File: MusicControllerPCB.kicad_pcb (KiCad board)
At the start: 2 copper layers, 66 x 55.9 mm, 8 parts, among them SW1 SW_Push, SW2 SW_Push, SW3 SW_Push, SW4 SW_Push

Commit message: Some cleanup
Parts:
- removed A1: Arduino_Nano_v3.x, Module:Arduino_Nano
- added A101: Arduino_Nano_v3.x, Module:Arduino_Nano, B.Cu at (89.6, 72.2)
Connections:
- Brd1 pad 1: Net-(A1-+5V) -> GND
- Brd1 pad 2: Net-(A1-A5) -> +5V
- Brd1 pad 3: Net-(A1-A5) -> Net-(A101-A5)
- Brd1 pad 4: Net-(A1-A5) -> Net-(A101-A4)
- RotaryEncoder1 pad 1: Net-(A1-D11) -> /Rot_{CLK}
- RotaryEncoder1 pad 2: Net-(A1-D10) -> /Rot_{DT}
- RotaryEncoder1 pad 4: Net-(A1-A5) -> +5V
- RotaryEncoder1 pad 5: Net-(RotaryEncoder1-GND) -> GND
- SW1 pad 1: Net-(A1-+5V) -> GND
- SW2 pad 1: Net-(A1-+5V) -> GND
- SW3 pad 1: Net-(A1-+5V) -> GND
- SW4 pad 1: Net-(A1-+5V) -> GND
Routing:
- net Net-(A1-A5): track 164.1 -> 0.00 mm
- net Net-(A1-+5V): track 129.3 -> 0.00 mm
- net +5V: track 0.00 -> 74.6 mm
- net /Rot_{DT}: track 0.00 -> 74.0 mm
- net /Rot_{CLK}: track 0.00 -> 60.0 mm
- net Net-(A1-D10): track 41.7 -> 0.00 mm
- net Net-(RotaryEncoder1-GND): track 40.8 -> 0.00 mm
- net Net-(A1-D11): track 40.8 -> 0.00 mm
- net Net-(A101-A5): track 0.00 -> 31.1 mm
- net Net-(A101-A4): track 0.00 -> 28.7 mm
- net Net-(A101-D2): track 24.4 -> 46.1 mm
- net Net-(A101-D3): track 17.4 -> 29.3 mm
- net Net-(A101-D5): track 23.6 -> 14.8 mm
- net Net-(A101-D4): track 35.3 -> 40.7 mm
- added copper zone on B.Cu, net GND
- added copper zone on F.Cu, net GND
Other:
- board text added: "- Use bigger traces - Use zones for GND on top/bottom"

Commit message: Added export
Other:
- board text added: "- Use bigger traces - Use zones for GND on top/bottom - Run the Design Rule Check once a while"
- board text removed: "- Use bigger traces - Use zones for GND on top/bottom"
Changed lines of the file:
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@@
     (effects (font (size 1 1) (thickness 0.15)) (justify left bottom))
   )
-  (gr_text "- Use bigger traces\n- Use zones for GND on top/bottom\n" (at 51 111) (layer "F.SilkS")
+  (gr_text "- Use bigger traces\n- Use zones for GND on top/bottom\n- Run the Design Rule Check once a while\n" (at 51 111) (layer "F.SilkS")
     (effects (font (size 1 1) (thickness 0.15)) (justify left bottom))
   )

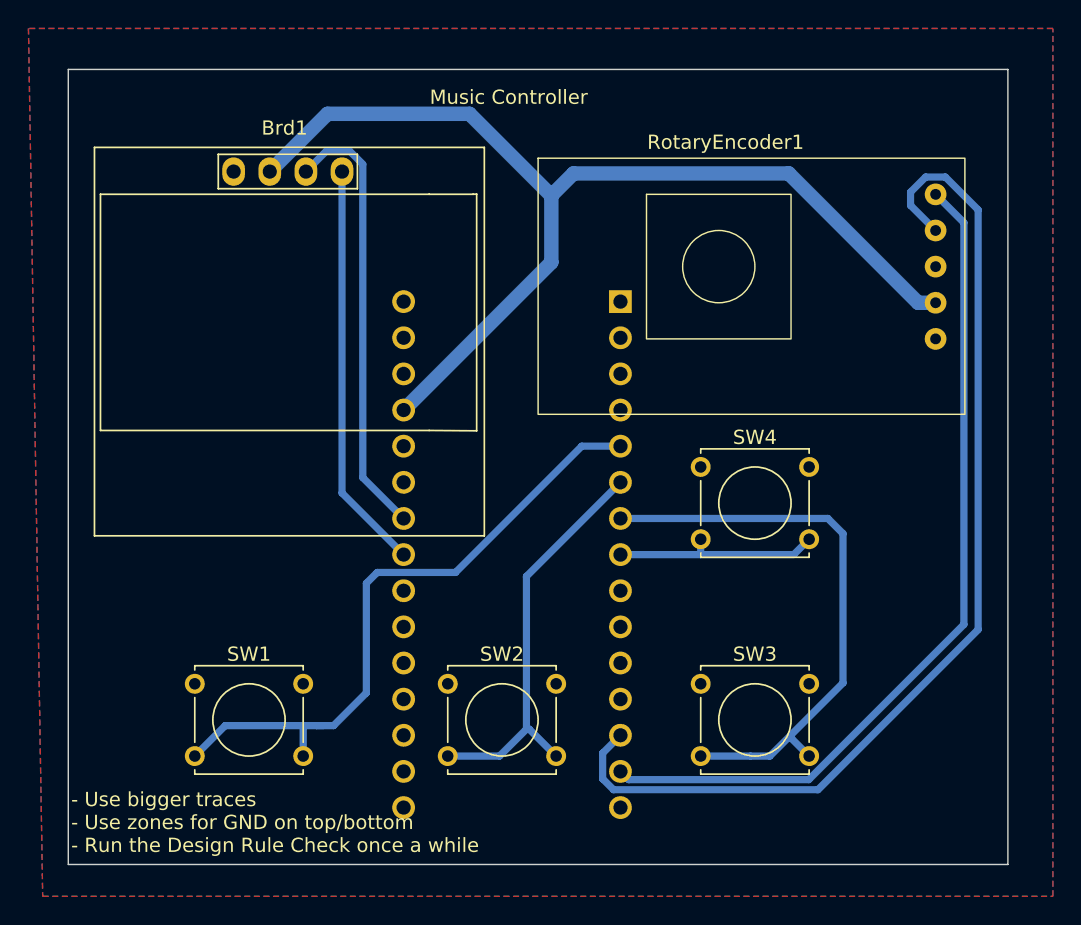
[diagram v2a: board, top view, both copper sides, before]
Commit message: Nano USB now faces North
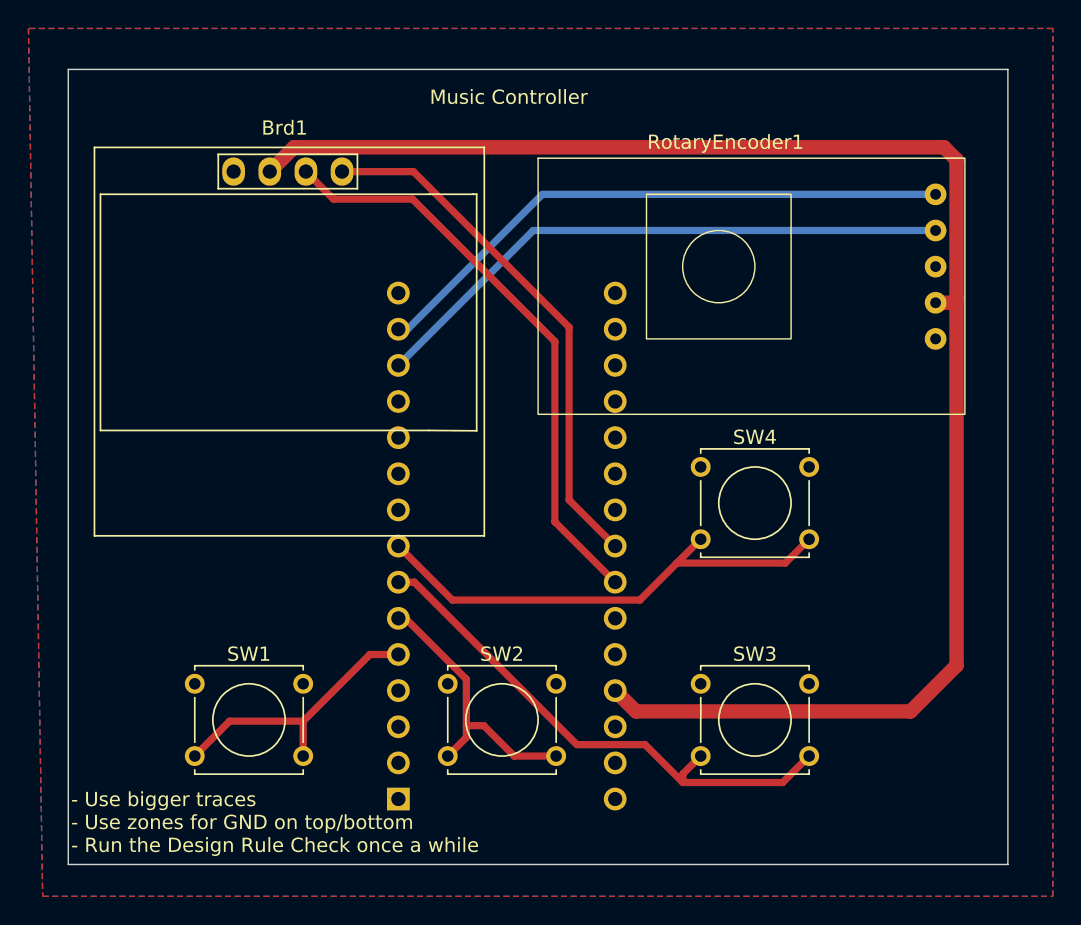
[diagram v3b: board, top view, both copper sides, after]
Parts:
- moved A101 38.3 mm to (74.0, 107.2), turned to 0 degrees
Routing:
- net +5V: track 74.6 -> 112.4 mm
- net /Rot_{DT}: track 74.0 -> 41.7 mm
- net Net-(A101-D2): track 46.1 -> 19.7 mm
- net Net-(A101-D5): track 14.8 -> 34.6 mm
- net /Rot_{CLK}: track 60.0 -> 41.7 mm
- net Net-(A101-A5): track 31.1 -> 41.1 mm
- net Net-(A101-D3): track 29.3 -> 19.7 mm
- net Net-(A101-A4): track 28.7 -> 37.2 mm
- net Net-(A101-D4): track 40.7 -> 37.9 mm
